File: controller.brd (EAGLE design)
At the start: 100 x 80 mm, 41 parts, among them IC1 7805DT, Q3 MOSFET-NCHANNELFDD8780, Q5 MMBT4403, U1 ATMEGA328P, Y1 16MHz

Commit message: completed RTC and micro schematic. to do: switches
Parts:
- added C9: (no value), SparkFun-Capacitors:0805
- added U$10, U$9: (no value), jt_parts:RESISTOR-0805
- added U$11: (no value), adafruit:CR1220-THM
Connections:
- removed net SERIALIN: JP1.5
- new net SCL: U$10.1, U$2.6, U1.28
- new net SDA: U$2.5, U$9.1, U1.27
- new net SERIAL: JP1.5, U1.12
- new net SQW: U$2.7
- new net VBATT: U$11.+2, U$2.3
- net 5V: now also C9.1, U$10.2, U$2.8, U$9.2
- net GND: now also C9.2, U$11.-, U$2.4
- net RCK: now also U1.13
- net SCK: now also U1.15
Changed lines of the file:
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@@
 </element>
 <element name="U$8" library="jt_parts" package="RESISTOR-0805" value="" x="-46.99" y="-66.04"/>
+<element name="C9" library="SparkFun-Capacitors" package="0805" value="" x="-52.07" y="-64.77"/>
+<element name="U$9" library="jt_parts" package="RESISTOR-0805" value="" x="-50.8" y="-69.85"/>
+<element name="U$10" library="jt_parts" package="RESISTOR-0805" value="" x="-50.8" y="-73.66"/>
+<element name="U$11" library="adafruit" package="CR1220-THM" value="" x="-44.45" y="-82.55"/>
 </elements>
 <signals>
@@
 <contactref element="S6" pad="2"/>
 <contactref element="S6" pad="1"/>
+<contactref element="U$2" pad="4"/>
+<contactref element="C9" pad="2"/>
+<contactref element="U$11" pad="-"/>
+<wire x1="-51.17" y1="-64.77" x2="-44.45" y2="-82.55" width="0" layer="19" extent="1-1"/>
+<wire x1="-48.26" y1="-57.785" x2="-51.17" y2="-64.77" width="0" layer="19" extent="1-1"/>
 <wire x1="-43.18" y1="-57.785" x2="-48.26" y2="-57.785" width="0" layer="19" extent="1-1"/>
 <wire x1="-45.49" y1="-50.8" x2="-43.18" y2="-57.785" width="0" layer="19" extent="1-1"/>
@@
 <wire x1="8.89" y1="46.99" x2="24.05614375" y2="42.2632" width="0" layer="19" extent="1-1"/>
 <wire x1="9.144" y1="49.53" x2="8.89" y2="46.99" width="0" layer="19" extent="1-1"/>
-<wire x1="68.41" y1="24.13" x2="40.64" y2="21.209" width="0" layer="19" extent="1-1"/>
+<wire x1="50.165" y1="43.1038" x2="36.83" y2="29.21" width="0" layer="19" extent="1-1"/>
+<wire x1="68.41" y1="24.13" x2="50.165" y2="43.1038" width="0" layer="19" extent="1-1"/>
 <wire x1="70.89" y1="23.12" x2="68.41" y2="24.13" width="0" layer="19" extent="1-1"/>
 <wire x1="69.977" y1="21.209" x2="70.89" y2="23.12" width="0" layer="19" extent="1-1"/>
@@
 <signal name="RCK">
 <contactref element="JP1" pad="4"/>
+<contactref element="U1" pad="13"/>
+<wire x1="22.86" y1="8.636" x2="31.25816875" y2="41.697515625" width="0" layer="19" extent="1-1"/>
 </signal>
 <signal name="SCK">
 <contactref element="JP1" pad="3"/>
+<contactref element="U1" pad="15"/>
+<wire x1="20.32" y1="8.89" x2="32.3895375" y2="42.828884375" width="0" layer="19" extent="1-1"/>
 </signal>
 <signal name="5V" class="2">
@@
 <contactref element="U1" pad="4"/>
 <contactref element="U$8" pad="1"/>
+<contactref element="C9" pad="1"/>
+<contactref element="U$2" pad="8"/>
+<contactref element="U$9" pad="2"/>
+<contactref element="U$10" pad="2"/>
+<wire x1="-49.8" y1="-69.85" x2="-49.8" y2="-73.66" width="0" layer="19" extent="1-1"/>
+<wire x1="-47.99" y1="-66.04" x2="-49.8" y2="-69.85" width="0" layer="19" extent="1-1"/>
+<wire x1="-52.97" y1="-64.77" x2="-47.99" y2="-66.04" width="0" layer="19" extent="1-1"/>
 <wire x1="-45.99" y1="-55.88" x2="-47.99" y2="-66.04" width="0" layer="19" extent="1-1"/>
 <wire x1="-41.54" y1="-45.72" x2="-45.99" y2="-55.88" width="0" layer="19" extent="1-1"/>
@@
 <wire x1="24.621828125" y1="41.697515625" x2="25.7532" y2="40.56614375" width="0" layer="19" extent="1-1"/>
 <wire x1="32.3895375" y1="46.0711125" x2="25.7532" y2="40.56614375" width="0" layer="19" extent="1-1"/>
+<wire x1="46.355" y1="48.3362" x2="32.3895375" y2="46.0711125" width="0" layer="19" extent="1-1"/>
 </signal>
 <signal name="N$64">
@@
 <signal name="N$68">
 </signal>
-<signal name="SERIALIN">
+<signal name="SERIAL">
 <contactref element="JP1" pad="5"/>
+<contactref element="U1" pad="12"/>
+<wire x1="25.4" y1="8.89" x2="30.69248125" y2="41.131828125" width="0" layer="19" extent="1-1"/>
 </signal>
 <signal name="N$3">
@@
 <wire x1="24.621828125" y1="47.20248125" x2="-47.36" y2="-45.72" width="0" layer="19" extent="1-1"/>
 </signal>
+<signal name="VBATT">
+<contactref element="U$2" pad="3"/>
+<contactref element="U$11" pad="+2"/>
+<wire x1="48.895" y1="43.1038" x2="-37.846" y2="-82.55" width="0" layer="19" extent="1-1"/>
+</signal>
+<signal name="SQW">
+<contactref element="U$2" pad="7"/>
+</signal>
+<signal name="SCL">
+<contactref element="U$2" pad="6"/>
+<contactref element="U$10" pad="1"/>
+<contactref element="U1" pad="28"/>
+<wire x1="25.187515625" y1="47.76816875" x2="-51.8" y2="-73.66" width="0" layer="19" extent="1-1"/>
+<wire x1="48.895" y1="48.3362" x2="25.187515625" y2="47.76816875" width="0" layer="19" extent="1-1"/>
+</signal>
+<signal name="SDA">
+<contactref element="U$2" pad="5"/>
+<contactref element="U$9" pad="1"/>
+<contactref element="U1" pad="27"/>
+<wire x1="25.7532" y1="48.333853125" x2="-51.8" y2="-69.85" width="0" layer="19" extent="1-1"/>
+<wire x1="50.165" y1="48.3362" x2="25.7532" y2="48.333853125" width="0" layer="19" extent="1-1"/>
+</signal>
 </signals>

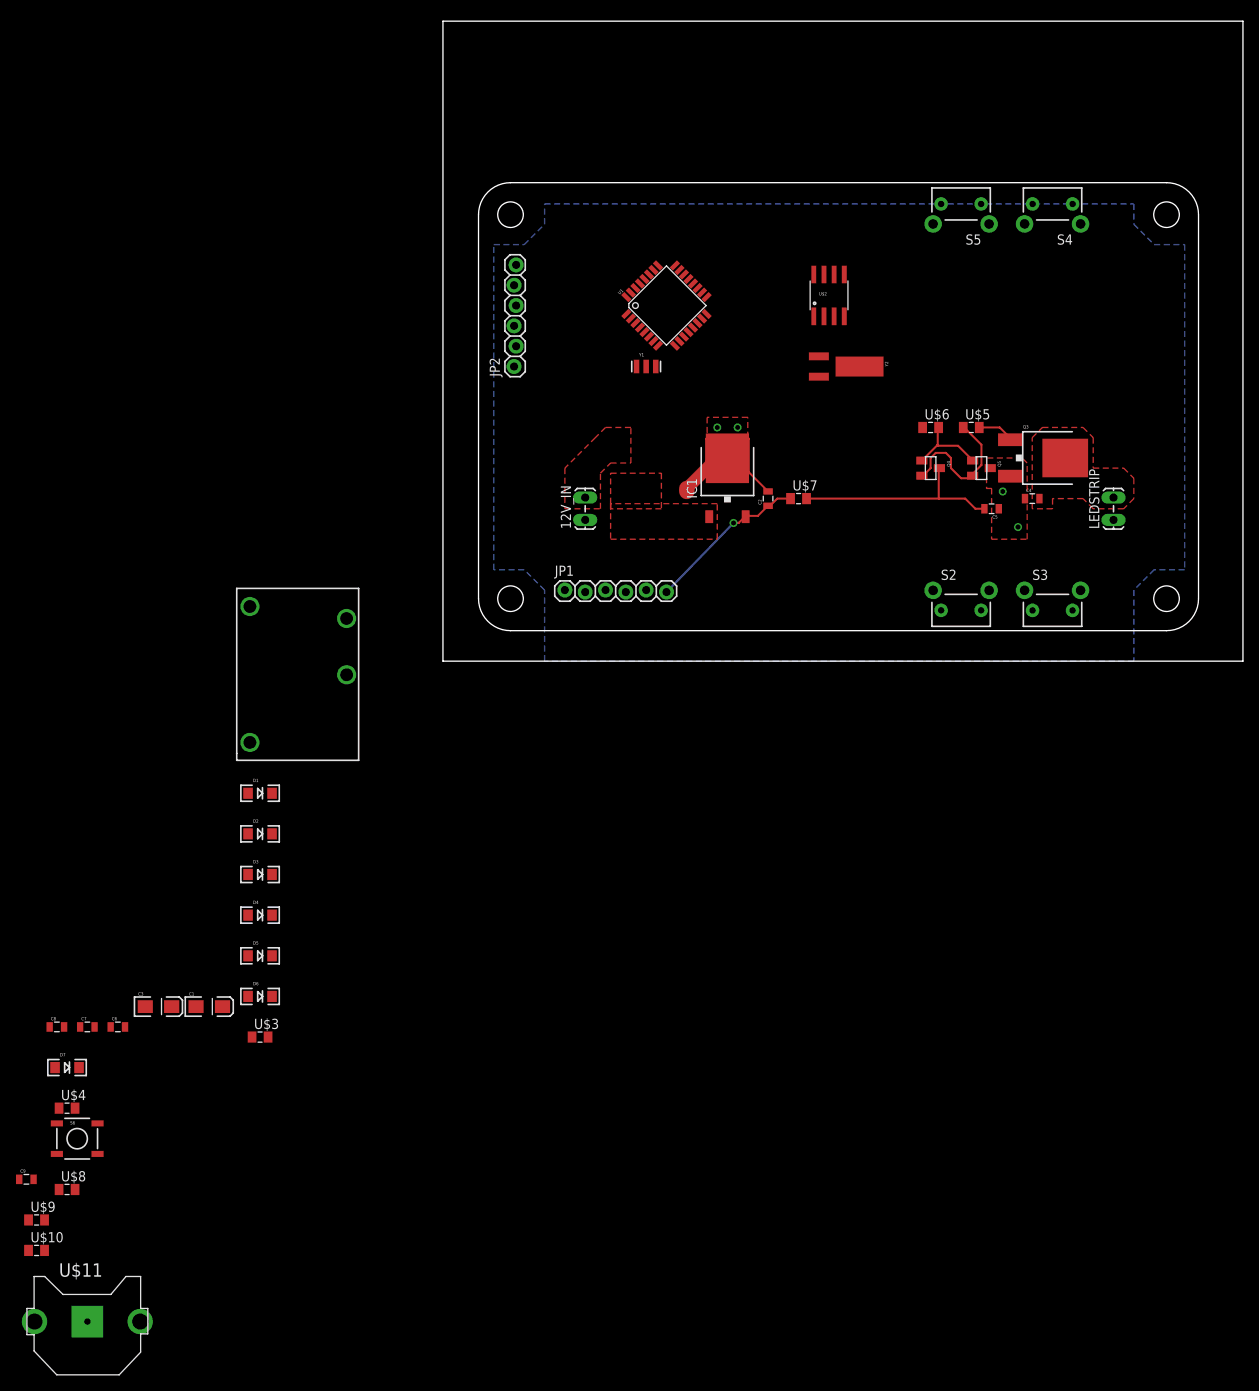
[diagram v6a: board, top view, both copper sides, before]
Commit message: Beginning of new controller board layout.
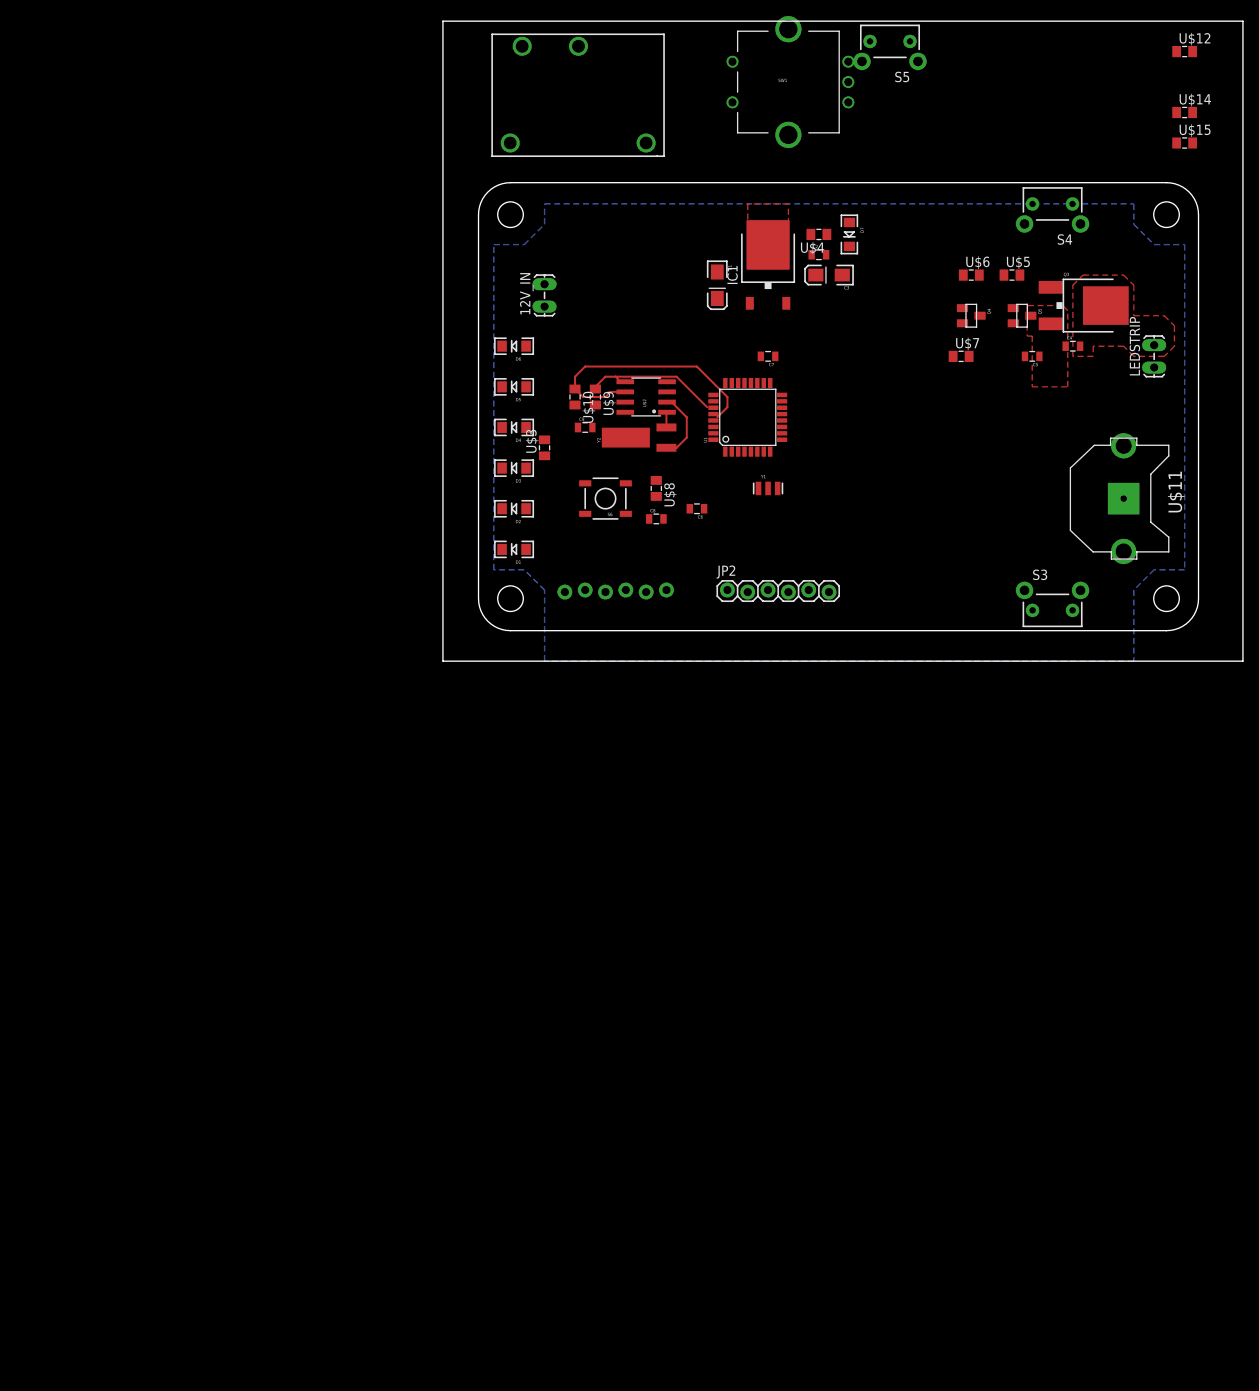
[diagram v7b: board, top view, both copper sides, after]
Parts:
- removed FRAME1: FRAME-LEDGER, SparkFun-Aesthetics:CREATIVE_COMMONS
- removed S2: SWITCH-MOMENTARY-2SIDE_EZ, SparkFun-Electromechanical:TACTILE-PTH-SIDEEZ
- added FRAME2: FRAME-LETTER, SparkFun-Aesthetics:CREATIVE_COMMONS
- added SW1: ROTARTY_ENCODER, SparkFun-Electromechanical:ROTARY_ENC_PLAIN
- added U$12, U$14, U$15: (no value), jt_parts:RESISTOR-0805
- moved U$11 165.4 mm to (85.1, 20.3), turned to 270 degrees
- moved U$4 144.1 mm to (47.0, 53.3), turned to 180 degrees
- moved D7 142.9 mm to (50.8, 53.3), turned to 270 degrees
- moved U$10 126.1 mm to (16.5, 33.0), turned to 270 degrees
- moved U$9 124.3 mm to (19.1, 33.0), turned to 270 degrees
- moved C3 124.0 mm to (48.3, 48.3), turned to 180 degrees
- moved C7 119.4 mm to (40.6, 38.1), turned to 180 degrees
- moved C9 117.1 mm to (17.8, 29.2)
- moved U$8 114.5 mm to (26.7, 21.6), turned to 270 degrees
- moved C1 110.3 mm to (34.3, 47.0), turned to 270 degrees
- moved S6 103.7 mm to (20.3, 20.3), turned to 180 degrees
- moved C8 98.2 mm to (26.7, 17.8)
- moved C6 97.1 mm to (31.8, 19.1), turned to 180 degrees
- moved S1 89.8 mm to (25.4, 64.8), turned to 90 degrees
- moved D6 87.3 mm to (8.89, 39.4), turned to 180 degrees
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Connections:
- new net N$13: S3.1, U$12.1
- new net N$16: S4.1, U$14.1
- new net N$17: S5.1, U$15.1
- new net N$18: U1.32
- new net N$19: U1.2
- new net N$20: U1.11
- net 5V: now also U$14.2, U$15.2; no longer U$7.1
- net GND: now also S3.2, S4.2, S5.2
- net RXI: now also U1.30
- net TXO: now also U1.31
- net VCC: now also U$12.2, U$7.1
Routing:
- net SCL: track 0.00 -> 32.7 mm
- net N$2: track 26.7 -> 0.00 mm
- net GND: track 26.7 -> 0.00 mm, vias 4 -> 0
- net 5V: track 20.3 -> 0.00 mm, vias 1 -> 0
- net N$5: track 18.0 -> 0.00 mm
- net SDA: track 0.00 -> 17.8 mm
- net NONE: track 10.3 -> 0.00 mm
- net N$7: track 0.00 -> 8.86 mm
- net N$3: track 4.63 -> 0.00 mm
- net N$6: track 0.00 -> 1.94 mm
- net 12V-RETURN: track 1.28 -> 0.00 mm
- removed copper zone on layer 1, net 12V
- removed copper zone on layer 1, net 12V-IN

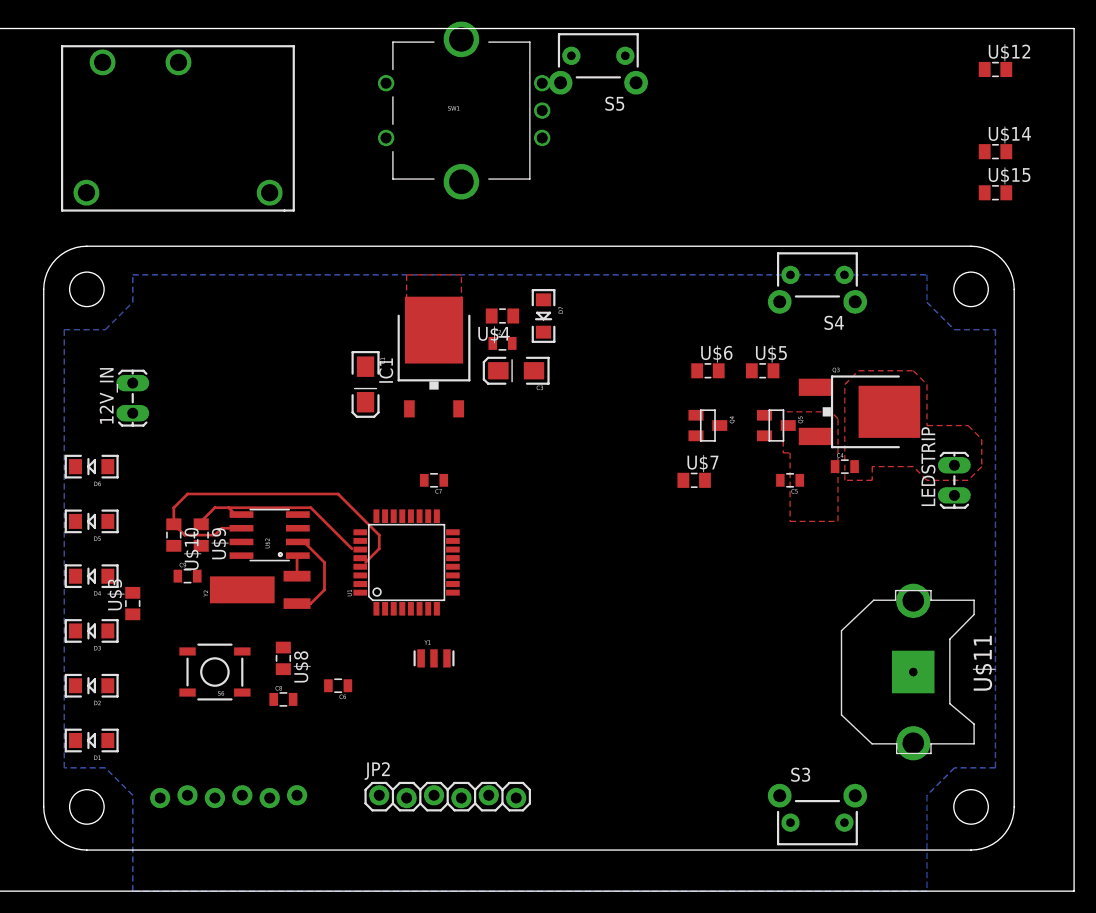
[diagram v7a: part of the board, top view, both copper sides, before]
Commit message: Layed out micro, jumpers, and rtc section.
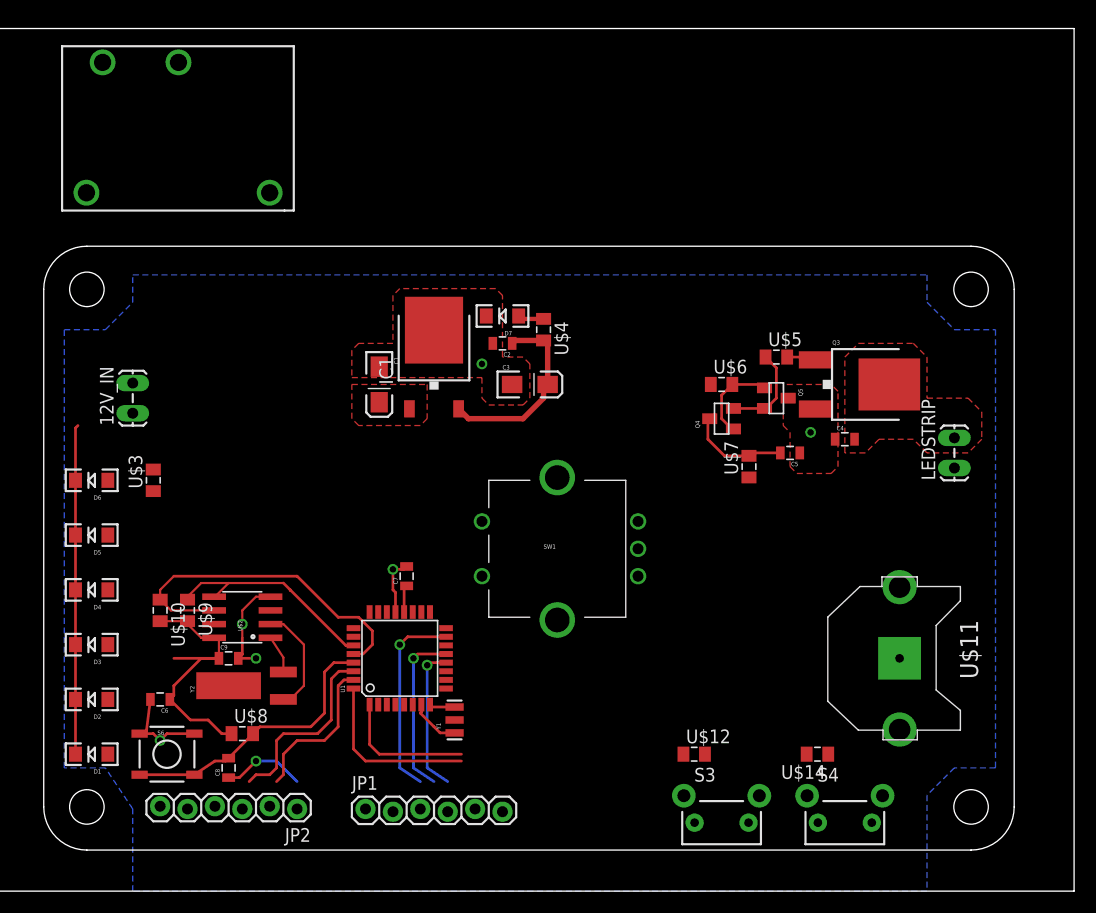
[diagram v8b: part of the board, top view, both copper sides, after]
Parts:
- removed S5: SWITCH-MOMENTARY-2SIDE_EZ, SparkFun-Electromechanical:TACTILE-PTH-SIDEEZ
- removed U$15: (no value), jt_parts:RESISTOR-0805
- moved FRAME2 94.5 mm to (16.5, -16.5)
- moved U$12 69.4 mm to (64.8, 12.7)
- moved U$14 58.3 mm to (76.2, 12.7), turned to 180 degrees
- moved S4 50.9 mm to (78.7, 6.35), turned to 0 degrees
- moved SW1 41.6 mm to (52.1, 31.8)
- moved C6 16.6 mm to (15.2, 17.8)
- moved U$3 11.6 mm to (14.6, 38.1)
- moved C7 9.25 mm to (38.1, 29.2), turned to 90 degrees
- moved Y2 8.98 mm to (26.7, 19.1)
- moved U1 8.91 mm to (37.5, 21.6)
- moved S3 8.89 mm to (67.3, 6.35)
- moved S6 8.82 mm to (15.9, 12.7), turned to 0 degrees
- moved C9 8.52 mm to (21.6, 21.6)
- moved C8 8.13 mm to (21.6, 11.4), turned to 90 degrees
- moved U$2 8.03 mm to (22.9, 25.4)
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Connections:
- removed net N$13: S3.1, U$12.1
- removed net N$16: S4.1, U$14.1
- removed net N$17: S5.1, U$15.1
- removed net N$18: U1.32
- removed net N$19: U1.2
- removed net N$20: U1.11
- new net ENC_A: SW1.A, U1.32
- new net ENC_B: SW1.B, U1.1
- new net SW1: S3.1, U$12.1, U1.10
- new net SW2: S4.1, U$14.1, U1.11
- net 5V: no longer JP1.6, U$15.2
- net GND: now also D1.C, D2.C, D3.C, D4.C, D5.C, D6.C; no longer S5.2
- net PWM: now also U1.9
- net VCC: now also JP1.6
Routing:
- net GND: track 0.00 -> 54.3 mm, vias 0 -> 6
- net 5V: track 0.00 -> 43.8 mm
- net N$15: track 0.00 -> 26.2 mm
- net SCK: track 0.00 -> 18.3 mm, vias 0 -> 1
- net RXI: track 0.00 -> 17.6 mm
- net ENC_A: track 0.00 -> 16.1 mm
- net RCK: track 0.00 -> 15.6 mm, vias 0 -> 1
- net TXO: track 0.00 -> 14.4 mm
- net SERIAL: track 0.00 -> 13.7 mm, vias 0 -> 1
- net ENC_B: track 0.00 -> 12.6 mm
- net N$2: track 0.00 -> 9.45 mm
- net N$5: track 0.00 -> 8.60 mm
- net NONE: track 0.00 -> 8.20 mm
- net DTR: track 0.00 -> 7.77 mm, vias 0 -> 1
- net N$1: track 0.00 -> 4.76 mm
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- added copper zone on layer 1, net 12V
